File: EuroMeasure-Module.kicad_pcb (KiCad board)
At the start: 2 copper layers, 100 x 100 mm, 38 parts, among them SW1 SW_DIP_x04, SW2 RST, U1 AZ1117-3V3, U2 STM32G030CxT, Y1 16MHz

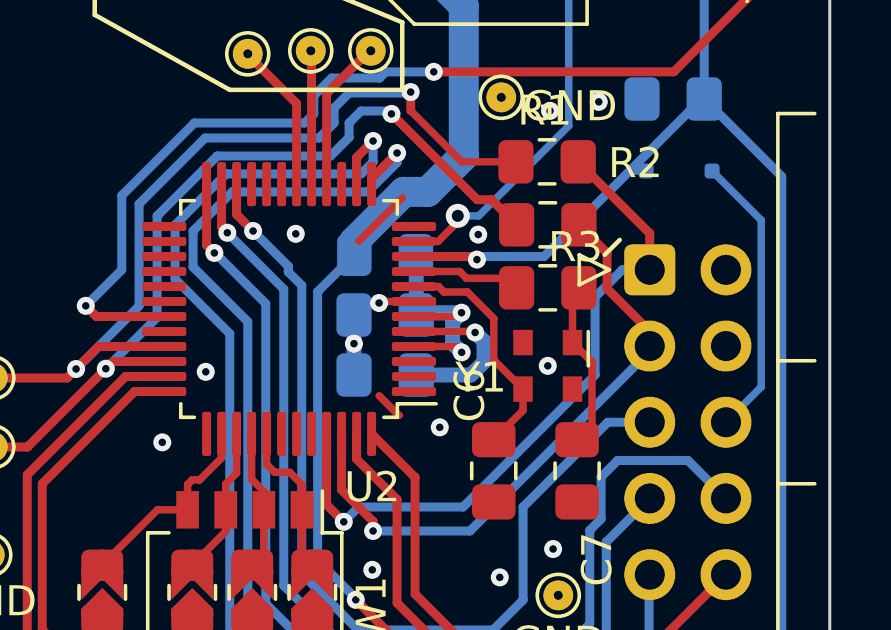
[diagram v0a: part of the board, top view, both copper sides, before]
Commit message: Fixed VREF
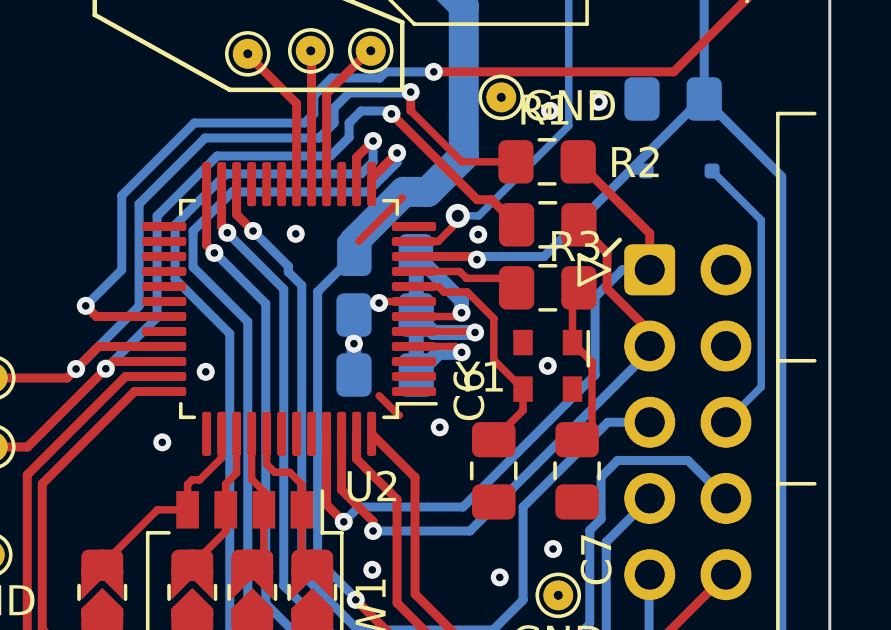
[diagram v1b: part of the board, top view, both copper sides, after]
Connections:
- C10 pad 1: /EuroMeasure/mcu_pwr -> /EuroMeasure/MCU_PWR
- C9 pad 1: /EuroMeasure/vref_c -> /EuroMeasure/MCU_PWR
- L1 pad 2: /EuroMeasure/mcu_pwr -> /EuroMeasure/MCU_PWR
- U2 pad 4: /EuroMeasure/mcu_pwr -> /EuroMeasure/MCU_PWR
- U2 pad 5: /EuroMeasure/vref_c -> /EuroMeasure/MCU_PWR
- U2 pad 6: /EuroMeasure/mcu_pwr -> /EuroMeasure/MCU_PWR
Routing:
- net /EuroMeasure/MCU_PWR: track 0.00 -> 16.1 mm, vias 0 -> 3
- net /EuroMeasure/mcu_pwr: track 8.43 -> 0.00 mm, vias 2 -> 0
- net /EuroMeasure/vref_c: track 5.56 -> 0.00 mm, vias 1 -> 0

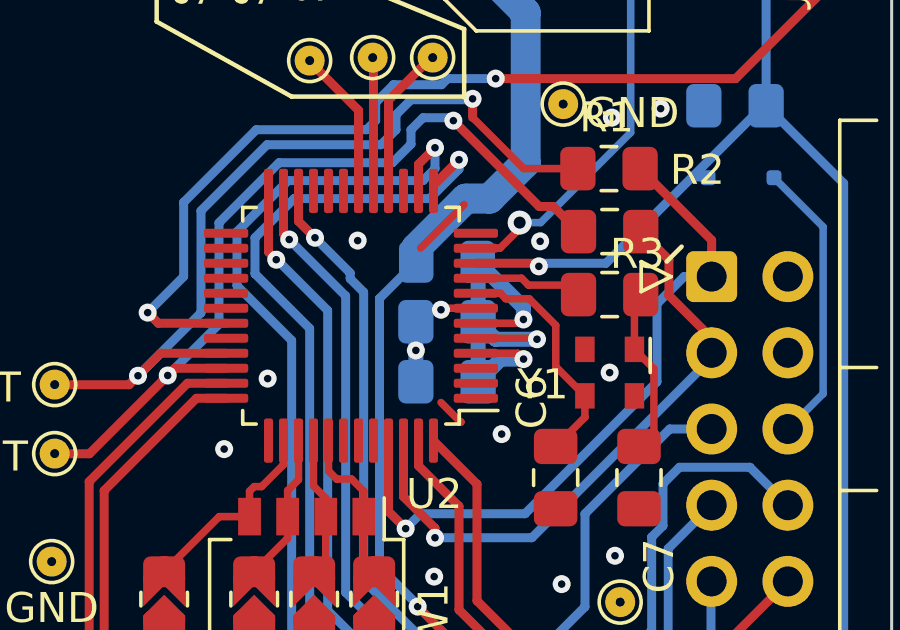
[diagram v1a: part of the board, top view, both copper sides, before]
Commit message: Updated DRC constraints
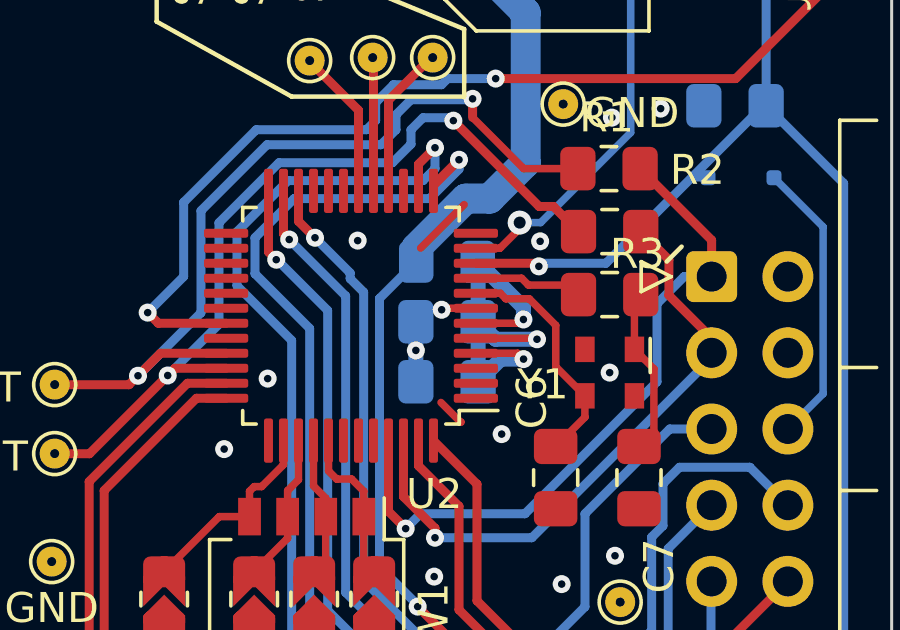
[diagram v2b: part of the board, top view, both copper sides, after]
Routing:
- net GND: track 35.5 -> 36.6 mm
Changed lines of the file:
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@@
       (height -4.91)
       (orientation 1)
-      (gr_text "128,7 mm" (at 59 100 90) (layer "User.7")
+      (gr_text "128.7 mm" (at 59 100 90) (layer "User.7")
         (effects (font (size 2 2) (thickness 0.15)))
       )
@@
   (segment (start 196.54 68.54) (end 194 68.54) (width 1) (layer "F.Cu") (net 2))
   (segment (start 184.3 90.05) (end 185.75 88.6) (width 0.25) (layer "F.Cu") (net 2))
-  (segment (start 185.0275 92.055) (end 184.9775 92.105) (width 0.25) (layer "F.Cu") (net 2))
   (segment (start 191.2275 79.305) (end 186.1275 74.205) (width 1) (layer "F.Cu") (net 2))
   (segment (start 185.0275 92.055) (end 186.14 92.055) (width 0.25) (layer "F.Cu") (net 2))
@@
   (via (at 190.6755 85.7) (size 0.6) (drill 0.25) (layers "F.Cu" "B.Cu") (free) (net 2))
   (via (at 192.3 85.4) (size 0.6) (drill 0.25) (layers "F.Cu" "B.Cu") (free) (net 2))
-  (via (at 184.9775 92.105) (size 0.6) (drill 0.25) (layers "F.Cu" "B.Cu") (net 2))
+  (via (at 185 92.105) (size 0.6) (drill 0.25) (layers "F.Cu" "B.Cu") (net 2))
   (via (at 190.7775 100.305) (size 0.6) (drill 0.25) (layers "F.Cu" "B.Cu") (net 2))
   (via (at 179.2 94.4) (size 0.6) (drill 0.25) (layers "F.Cu" "B.Cu") (free) (net 2))
@@
   (segment (start 184.14 94.505) (end 184.14 93.46) (width 0.5) (layer "B.Cu") (net 2))
   (segment (start 184.14 93.46) (end 184.14 92.505) (width 0.5) (layer "B.Cu") (net 2))
+  (segment (start 184.54 92.105) (end 184.14 92.505) (width 0.25) (layer "B.Cu") (net 2))
+  (segment (start 185.09 92.105) (end 184.54 92.105) (width 0.25) (layer "B.Cu") (net 2))
   (segment (start 193.5525 74.0675) (end 194 73.62) (width 1) (layer "B.Cu") (net 2))
   (segment (start 194 73.62) (end 196.54 73.62) (width 1) (layer "B.Cu") (net 2))
@@
   (segment (start 188.1775 93.088631) (end 186.798631 93.088631) (width 0.5) (layer "B.Cu") (net 53))
   (segment (start 187.729305 93.750693) (end 186.969307 93.750693) (width 0.5) (layer "B.Cu") (net 53))
-  (segment (start 186.290849 92.429151) (end 186.215 92.505) (width 0.5) (layer "B.Cu") (net 53))
   (segment (start 186.798631 93.088631) (end 186.215 92.505) (width 0.5) (layer "B.Cu") (net 53))
   (segment (start 186.215 92.505) (end 186.215 90.5175) (width 0.5) (layer "B.Cu") (net 53))
